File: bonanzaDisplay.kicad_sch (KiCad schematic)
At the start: 75 parts, among them J1 OLED-1.31-SSD1322, J15 SWD, J5 Conn_01x10, J6 USB_C_Receptacle_USB2.0, SW1 TS-1088-AR02016, SW2 TS-1088-AR02016, SW3 SIQ-02FVS3_C41430892, U1 RP2354A, U2 XC6206P302MR, U3 XC6206P282MR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

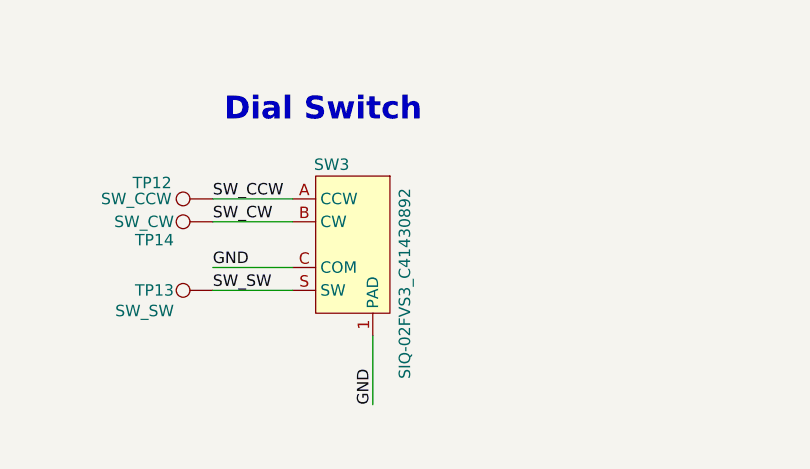
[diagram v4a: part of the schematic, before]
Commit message: DRC pass, updated BOM
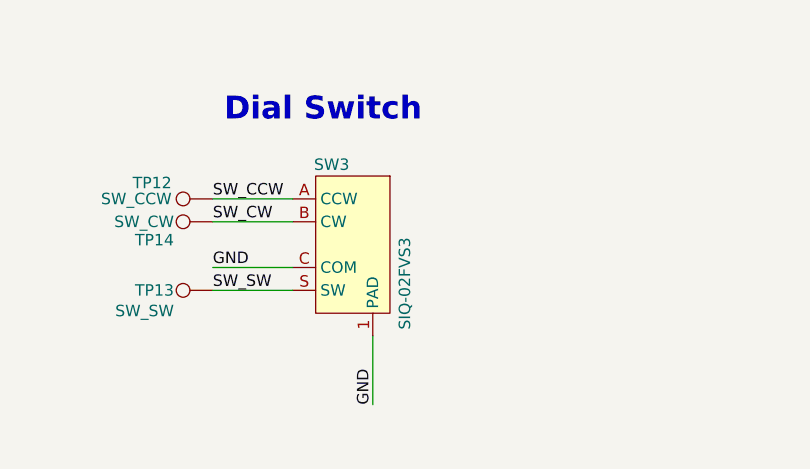
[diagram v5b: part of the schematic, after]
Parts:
- C14, C15, C18, C21, C24, C26: MPN GRM155R60J475ME87D -> (none); PARTNO (none) -> CL05A475KP5NRNC; Supplier LCSC -> (none)
- C16, C17: MPN GRM1555C1E100JA01D -> (none); PARTNO (none) -> GRM1555C1E100JA01D
- C19, C35: PARTNO (none) -> GRM155R71H104KE14D
- C20, C23, C25, C27, C28, C30, C31, C32, C33, C41: MPN GRM155R71C104KA88J -> (none); PARTNO (none) -> GRM155R71H104KE14D; Supplier Mouser -> (none)
- C22, C38, C39, C40: PARTNO (none) -> CL05A105KO5NNNC
- C29: LCSC (none) -> C106862; PARTNO (none) -> CC0402KRX7R9BB333
- C34: LCSC (none) -> C602037
- C36: PARTNO (none) -> CL21A106KAYNNNE
- C37: LCSC (none) -> C77020; PARTNO (none) -> GRM155R71H104KE14D
- C8: LCSC (none) -> C15850; PARTNO MSAST21GBB5106MTNA01 -> CL21A106KAYNNNE
- J1: PARTNO (none) -> AFC07-S30ECA-00
- L1: MPN MLP2016H3R3MT0S1 -> (none); PARTNO (none) -> MLP2016H3R3MT0S1
- R12: LCSC (none) -> C185428; PARTNO (none) -> RC0402FR-0730K9L
- R13: LCSC (none) -> C60490; PARTNO (none) -> RC0402FR-0710KL
- R14: LCSC (none) -> C274888; PARTNO (none) -> RC0402FR-0713K7L
- R2, R4: LCSC C25905 -> C105872; PARTNO (none) -> RC0402FR-075K1L
- R31, R37, R38: MPN RC0402FR-0727RL -> (none); PARTNO (none) -> RC0402FR-0727RL; Supplier LCSC -> (none)
- R32: MPN RC0402FR-071KL -> (none); PARTNO (none) -> RC0402FR-071KL; Supplier LCSC -> (none)
- R33: MPN RC0402FR-0710KL -> (none); PARTNO (none) -> RC0402FR-0710KL; Supplier LCSC -> (none)
- R34: PARTNO (none) -> RC0402FR-0751RL
- R35: PARTNO (none) -> RC0402FR-07590KL
- R39: LCSC C25900 -> C105871; PARTNO (none) -> RC0402FR-074K7L
- SW1, SW2: PARTNO (none) -> TS-1088-AR02016
- SW3: value SIQ-02FVS3_C41430892 -> SIQ-02FVS3; LCSC (none) -> C41430892; LCSC Part C29780879 -> (none); PARTNO (none) -> SIQ-02FVS3
- U1: PARTNO (none) -> RP2354A
- U4: LCSC (none) -> C3200405; LCSC Part C3200405 -> (none); PARTNO (none) -> TPS62933DRLR
- Y1: MPN ABM8-272-T3 -> (none); PARTNO (none) -> ABM8-272-T3

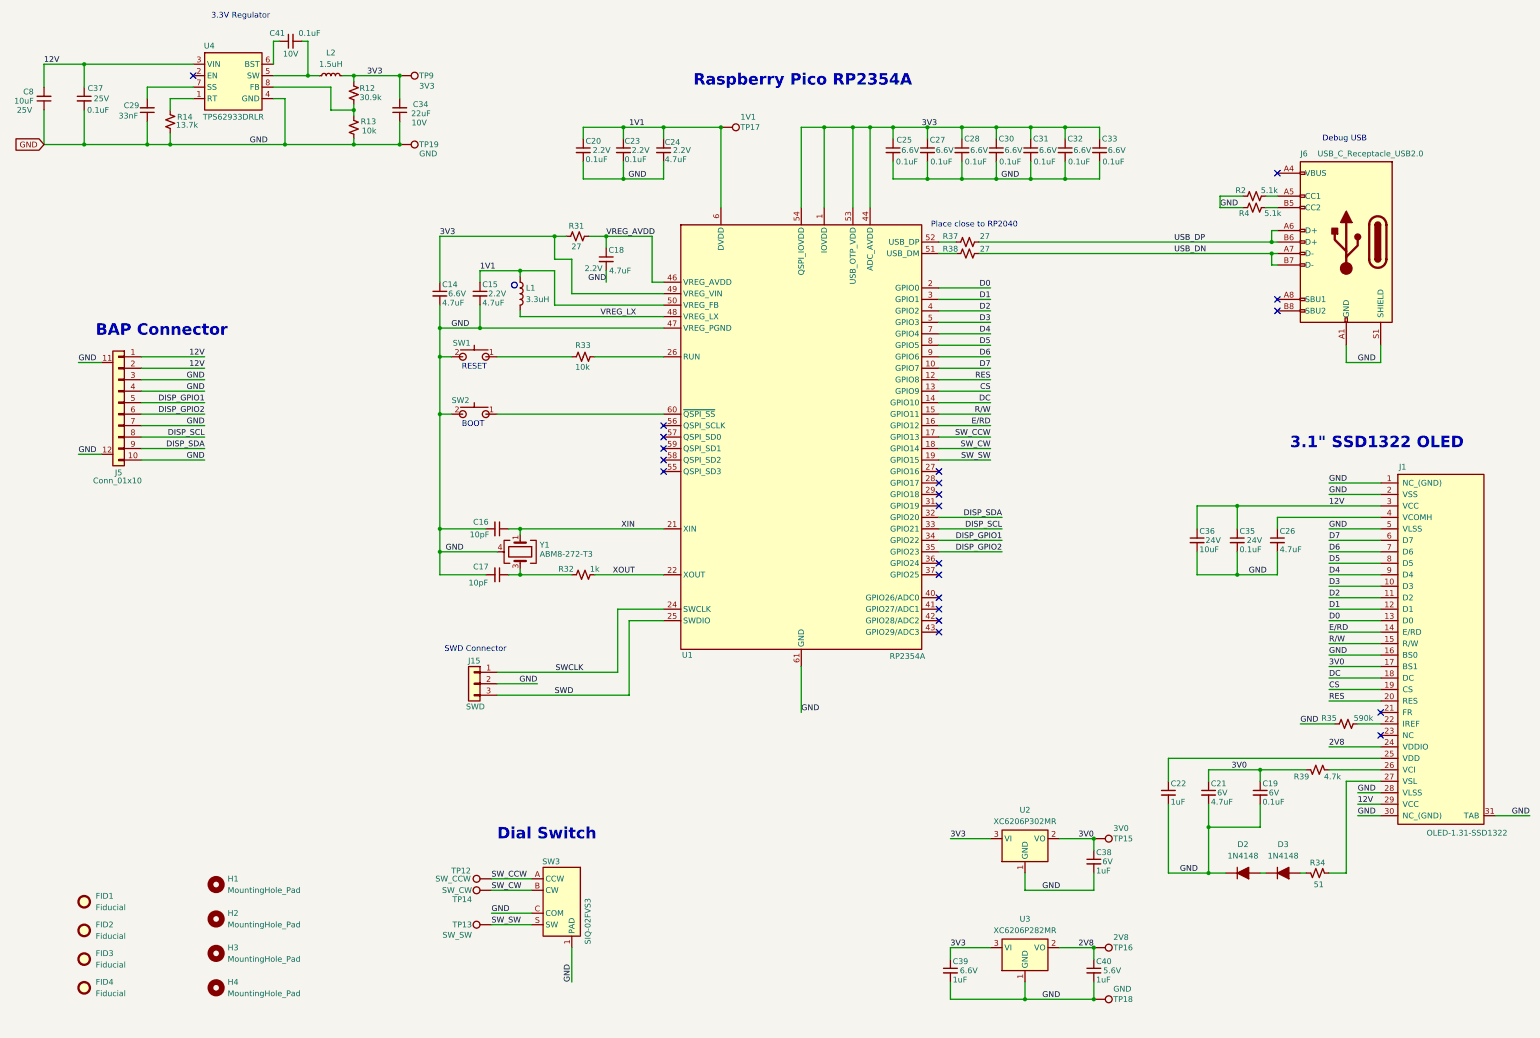
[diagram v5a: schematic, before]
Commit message: added manual 12V header
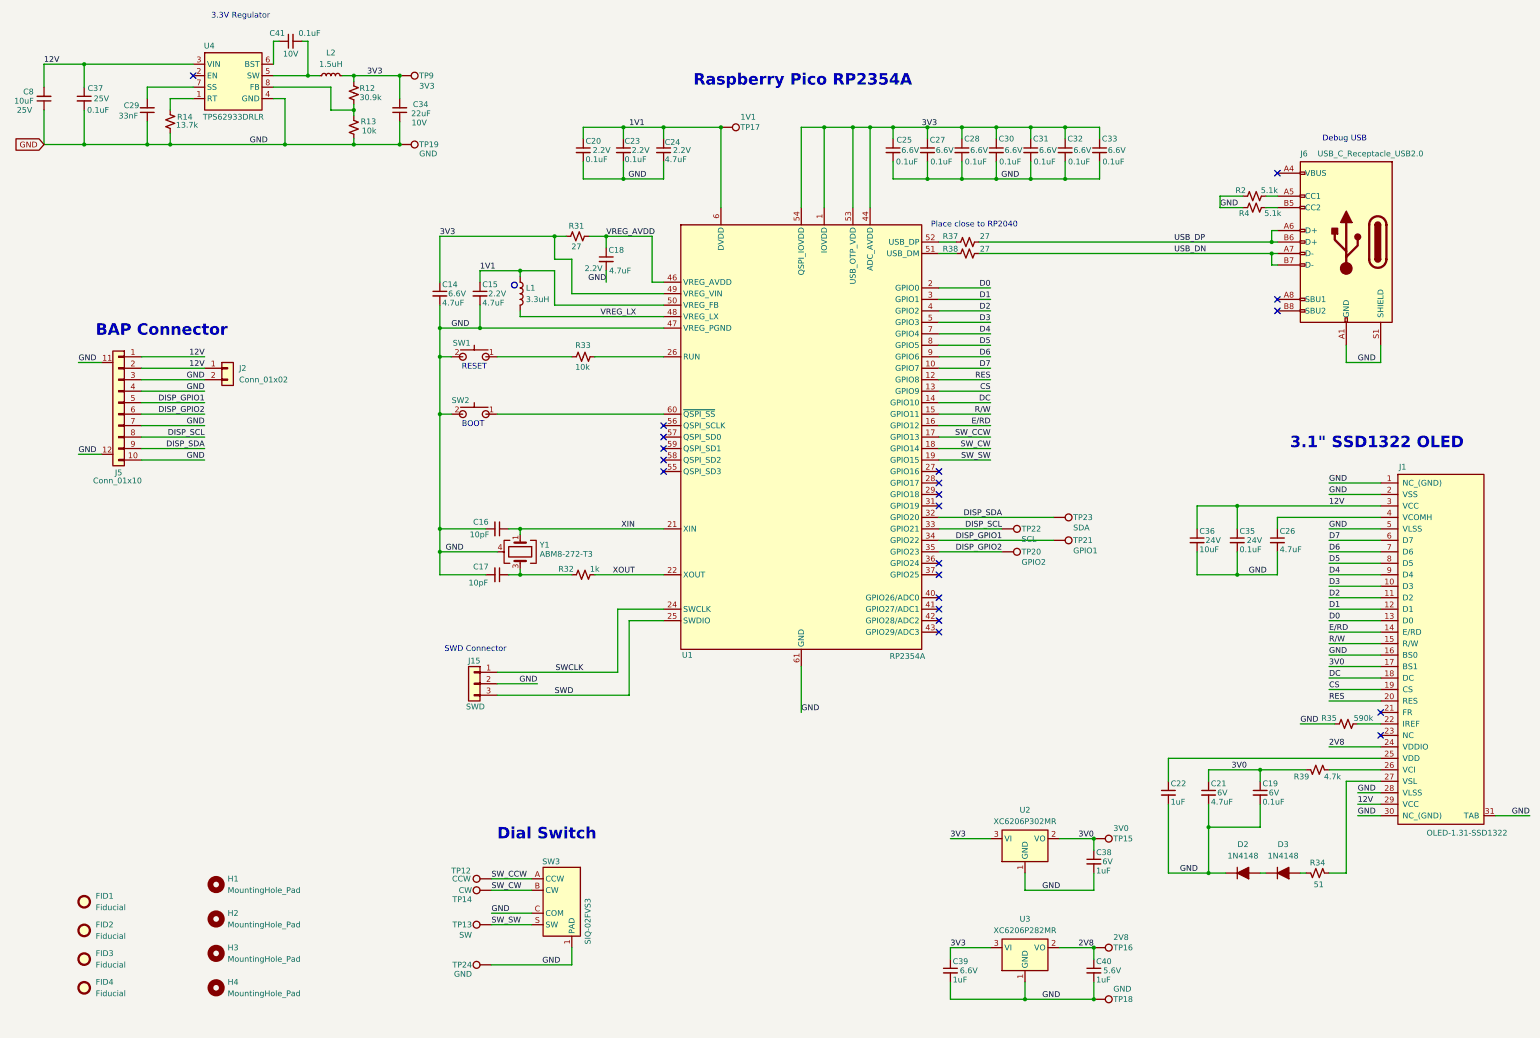
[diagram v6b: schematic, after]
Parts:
- added J2: Conn_01x02, Connector_PinHeader_2.54mm:PinHeader_1x02_P2.54mm_Vertical, symbol Connector_Generic:Conn_01x02
- added TP20: GPIO2, bonanzaDisplay:TestPoint_Pad_D1.0mm, symbol Connector:TestPoint
- added TP21: GPIO1, bonanzaDisplay:TestPoint_Pad_D1.0mm, symbol Connector:TestPoint
- added TP22: SCL, bonanzaDisplay:TestPoint_Pad_D1.0mm, symbol Connector:TestPoint
- added TP23: SDA, bonanzaDisplay:TestPoint_Pad_D1.0mm, symbol Connector:TestPoint
- added TP24: GND, bonanzaDisplay:TestPoint_Pad_D1.0mm, symbol Connector:TestPoint
- TP12: value SW_CCW -> CCW
- TP13: value SW_SW -> SW
- TP14: value SW_CW -> CW
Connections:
- net 12V: now also J2.1 (Pin_1)
- net DISP_GPIO1: now also TP21.1
- net DISP_GPIO2: now also TP20.1
- net DISP_SCL: now also TP22.1
- net DISP_SDA: now also TP23.1
- net GND: now also J2.2 (Pin_2), TP24.1

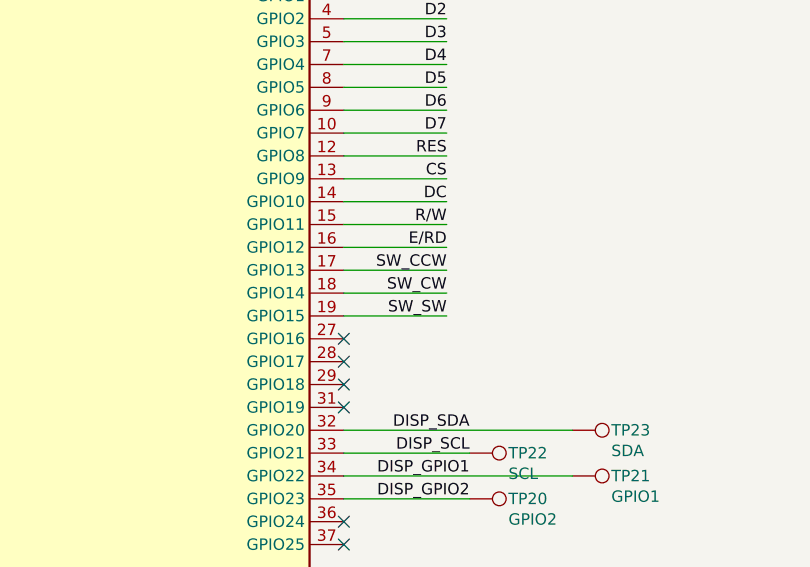
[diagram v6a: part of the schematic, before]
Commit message: test point arrangement
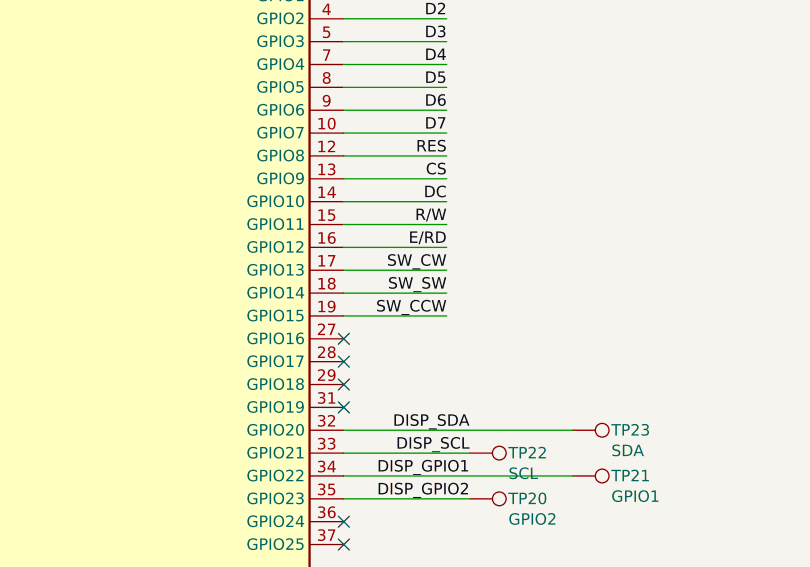
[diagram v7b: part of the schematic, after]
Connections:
- net SW_CCW: now also U1.19 (GPIO15); no longer U1.17 (GPIO13)
- net SW_CW: now also U1.17 (GPIO13); no longer U1.18 (GPIO14)
- net SW_SW: now also U1.18 (GPIO14); no longer U1.19 (GPIO15)

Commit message: updated BOM with some cheaper JLC Basic parts
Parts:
- C14, C15, C18, C21, C24, C26: LCSC C368809 -> C23733
- C16, C17: LCSC C161512 -> C32949; PARTNO GRM1555C1E100JA01D -> (none)
- C22, C38, C39, C40: LCSC C29266 -> C52923; PARTNO CL05A105KO5NNNC -> (none)
- C34: LCSC C602037 -> C45783
- C36, C8: PARTNO CL21A106KAYNNNE -> (none)
- R13, R33: LCSC C60490 -> C25744; PARTNO RC0402FR-0710KL -> (none)
- R2, R4: LCSC C105872 -> C25905; PARTNO RC0402FR-075K1L -> (none)
- R32: LCSC C106235 -> C11702; PARTNO RC0402FR-071KL -> (none)
- R39: LCSC C105871 -> C25900; PARTNO RC0402FR-074K7L -> (none)
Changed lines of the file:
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@@
 			)
 		)
-		(property "LCSC" "C105871"
+		(property "LCSC" "C25900"
 			(at 317.5 223.52 0)
 			(hide yes)
@@
 			)
 		)
-		(property "PARTNO" "RC0402FR-074K7L"
+		(property "PARTNO" ""
 			(at 317.5 200.66 90)
 			(hide yes)
@@
 			)
 		)
-		(property "LCSC" "C368809"
+		(property "LCSC" "C23733"
 			(at 240.03 83.82 0)
 			(hide yes)
@@
 			)
 		)
-		(property "PARTNO" "CL21A106KAYNNNE"
+		(property "PARTNO" ""
 			(at 290.83 149.86 0)
 			(hide yes)
@@
 			)
 		)
-		(property "LCSC" "C106235"
+		(property "LCSC" "C11702"
 			(at 154.94 157.48 0)
 			(hide yes)
@@
 			)
 		)
-		(property "PARTNO" "RC0402FR-071KL"
+		(property "PARTNO" ""
 			(at 154.94 157.48 90)
 			(hide yes)
@@
 			)
 		)
-		(property "LCSC" "C368809"
+		(property "LCSC" "C23733"
 			(at 154.94 109.22 0)
 			(hide yes)
@@
 			)
 		)
-		(property "LCSC" "C60490"
+		(property "LCSC" "C25744"
 			(at 154.94 109.22 0)
 			(hide yes)
@@
 			)
 		)
-		(property "PARTNO" "RC0402FR-0710KL"
+		(property "PARTNO" ""
 			(at 154.94 109.22 90)
 			(hide yes)
@@
 			)
 		)
-		(property "LCSC" "C368809"
+		(property "LCSC" "C23733"
 			(at 317.5 200.66 0)
 			(hide yes)
@@
 			)
 		)
-		(property "PARTNO" "RC0402FR-075K1L"
+		(property "PARTNO" ""
 			(at 303.53 76.2 0)
 			(hide yes)
@@
 			)
 		)
-		(property "LCSC" "C105872"
+		(property "LCSC" "C25905"
 			(at 303.53 76.2 0)
 			(hide yes)
@@
 			)
 		)
-		(property "LCSC" "C29266"
+		(property "LCSC" "C52923"
 			(at 267.97 245.11 0)
 			(hide yes)
@@
 			)
 		)
-		(property "PARTNO" "CL05A105KO5NNNC"
+		(property "PARTNO" ""
 			(at 267.97 245.11 0)
 			(hide yes)
@@
 			)
 		)
-		(property "PARTNO" "RC0402FR-0710KL"
+		(property "PARTNO" ""
 			(at 104.14 58.42 0)
 			(hide yes)
@@
 			)
 		)
-		(property "LCSC" "C60490"
+		(property "LCSC" "C25744"
 			(at 104.14 58.42 0)
 			(hide yes)
@@
 			)
 		)
-		(property "LCSC" "C161512"
+		(property "LCSC" "C32949"
 			(at 135.89 157.48 0)
 			(hide yes)
@@
 			)
 		)
-		(property "PARTNO" "GRM1555C1E100JA01D"
+		(property "PARTNO" ""
 			(at 135.89 157.48 90)
 			(hide yes)
@@
 			)
 		)
-		(property "PARTNO" "CL21A106KAYNNNE"
+		(property "PARTNO" ""
 			(at 35.56 52.07 90)
 			(hide yes)
@@
 			)
 		)
-		(property "LCSC" "C29266"
+		(property "LCSC" "C52923"
 			(at 267.97 220.98 0)
 			(hide yes)
@@
 			)
 		)
-		(property "PARTNO" "CL05A105KO5NNNC"
+		(property "PARTNO" ""
 			(at 267.97 220.98 0)
 			(hide yes)
@@
 			)
 		)
-		(property "LCSC" "C368809"
+		(property "LCSC" "C23733"
 			(at 172.72 63.5 0)
 			(hide yes)
@@
 			)
 		)
-		(property "LCSC" "C29266"
+		(property "LCSC" "C52923"
 			(at 284.48 205.74 0)
 			(hide yes)
@@
 			)
 		)
-		(property "PARTNO" "CL05A105KO5NNNC"
+		(property "PARTNO" ""
 			(at 284.48 205.74 0)
 			(hide yes)
@@
 			)
 		)
-		(property "LCSC" "C368809"
+		(property "LCSC" "C23733"
 			(at 160.02 87.63 0)
 			(hide yes)
@@
 			)
 		)
-		(property "LCSC" "C161512"
+		(property "LCSC" "C32949"
 			(at 135.89 147.32 0)
 			(hide yes)
@@
 			)
 		)
-		(property "PARTNO" "GRM1555C1E100JA01D"
+		(property "PARTNO" ""
 			(at 135.89 147.32 90)
 			(hide yes)
@@
 			)
 		)
-		(property "LCSC" "C602037"
+		(property "LCSC" "C45783"
 			(at 114.3 54.61 0)
 			(hide yes)
@@
 			)
 		)
-		(property "LCSC" "C29266"
+		(property "LCSC" "C52923"
 			(at 236.22 245.11 0)
 			(hide yes)
@@
 			)
 		)
-		(property "PARTNO" "CL05A105KO5NNNC"
+		(property "PARTNO" ""
 			(at 236.22 245.11 0)
 			(hide yes)
@@
 			)
 		)
-		(property "LCSC" "C368809"
+		(property "LCSC" "C23733"
 			(at 293.37 205.74 0)
 			(hide yes)
@@
 			)
 		)
-		(property "PARTNO" "RC0402FR-075K1L"
+		(property "PARTNO" ""
 			(at 303.53 73.66 0)
 			(hide yes)
@@
 			)
 		)
-		(property "LCSC" "C105872"
+		(property "LCSC" "C25905"
 			(at 303.53 73.66 0)
 			(hide yes)
